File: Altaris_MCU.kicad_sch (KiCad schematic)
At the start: 80 parts, among them J1 Screw_Terminal_01x02, J10 USB_C_Receptacle_USB2.0_16P, J11 Screw_Terminal_01x02, J2 Conn_01x04_Pin, J3 Screw_Terminal_01x02, J4 Screw_Terminal_01x02, J5 Conn_01x04_Pin, J6 Conn_01x04_Pin, J7 Conn_01x08_Socket, J8 Screw_Terminal_01x02, J9 USB_C_Receptacle_USB2.0_16P, Q1 Q_NMOS, SW2 RESET1, SW3 BOOT1, U1 ESP32-S3-WROOM-1, U10 USBLC6-2SC6, U11 MAX31855KASA, U12 TPS62827DMQT, U15 CH340X, U2 MAX31855KASA, U3 TPS79333-EP, U4 ICM-20948, U5 TPS79318-EP, U6 SN74AVC4T774RSVR, U7 MAX31855KASA, U8 MAX31855KASA, U9 SN74AVC4T774RSVR

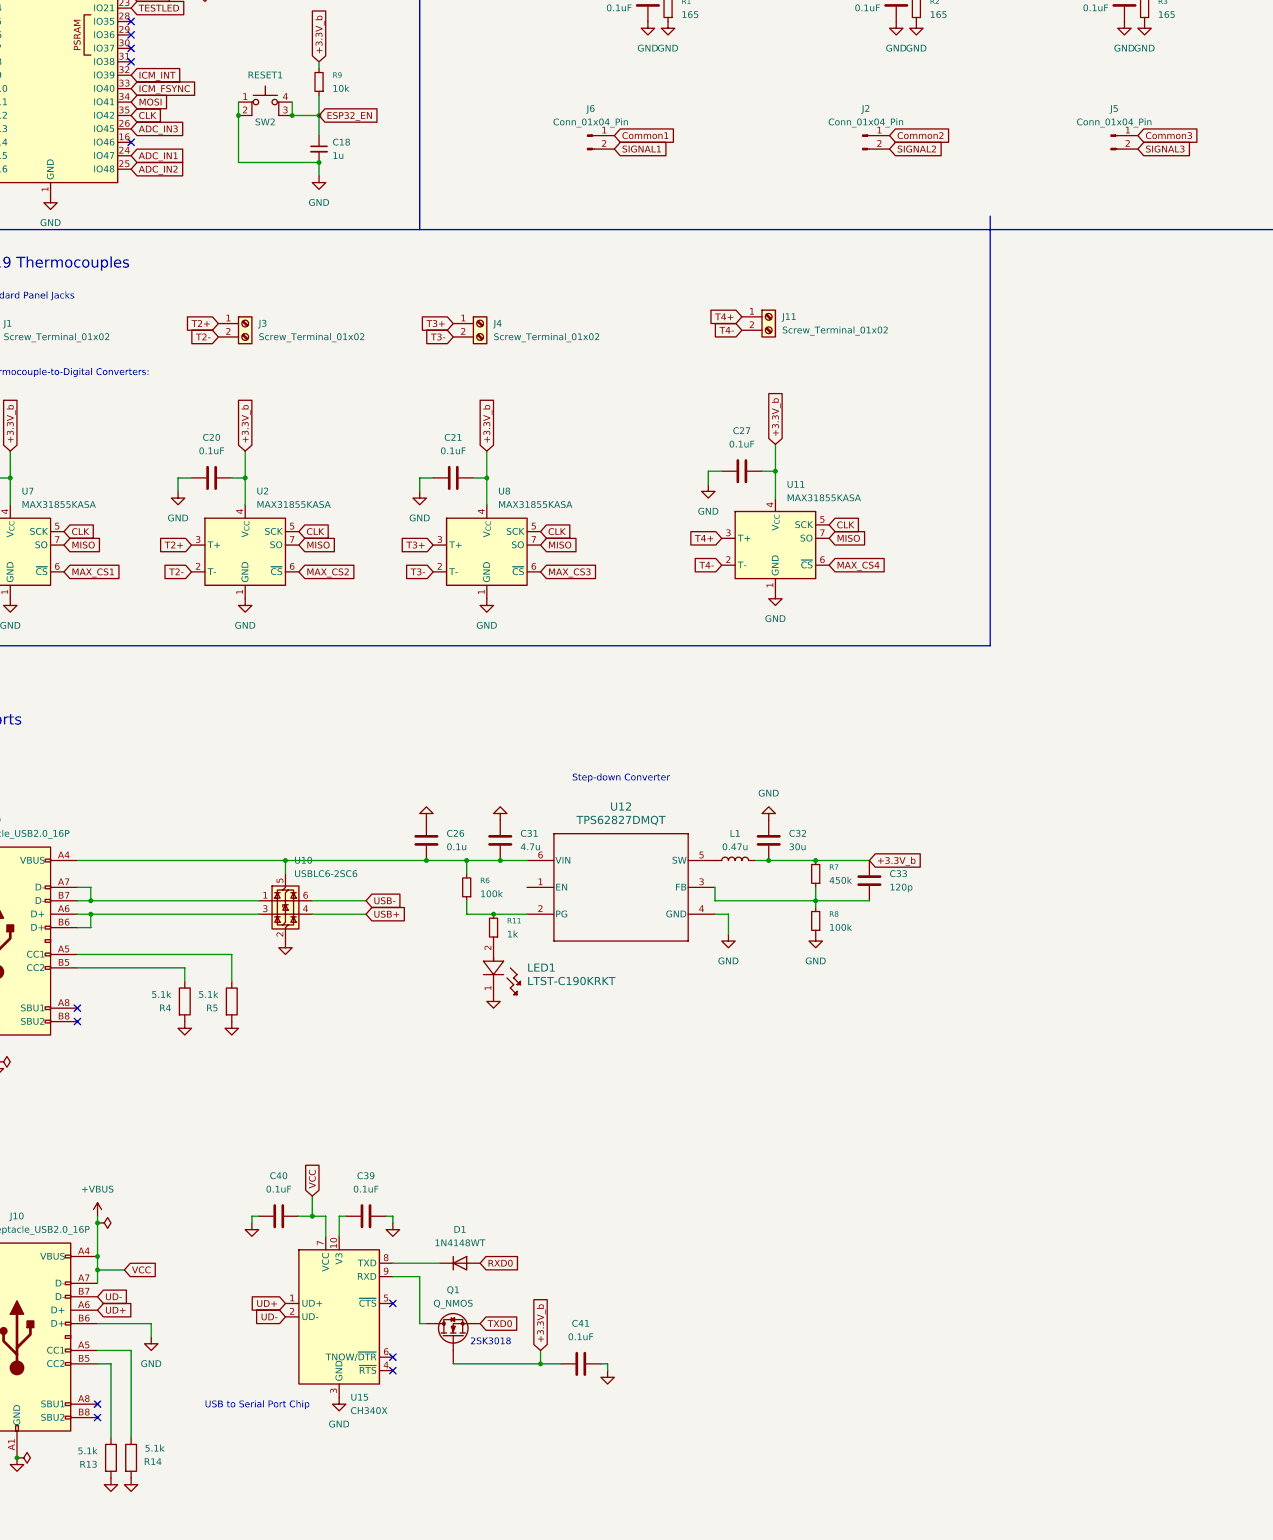
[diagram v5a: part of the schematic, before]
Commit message: Fixed second USB port wiring, changed to screw terminals
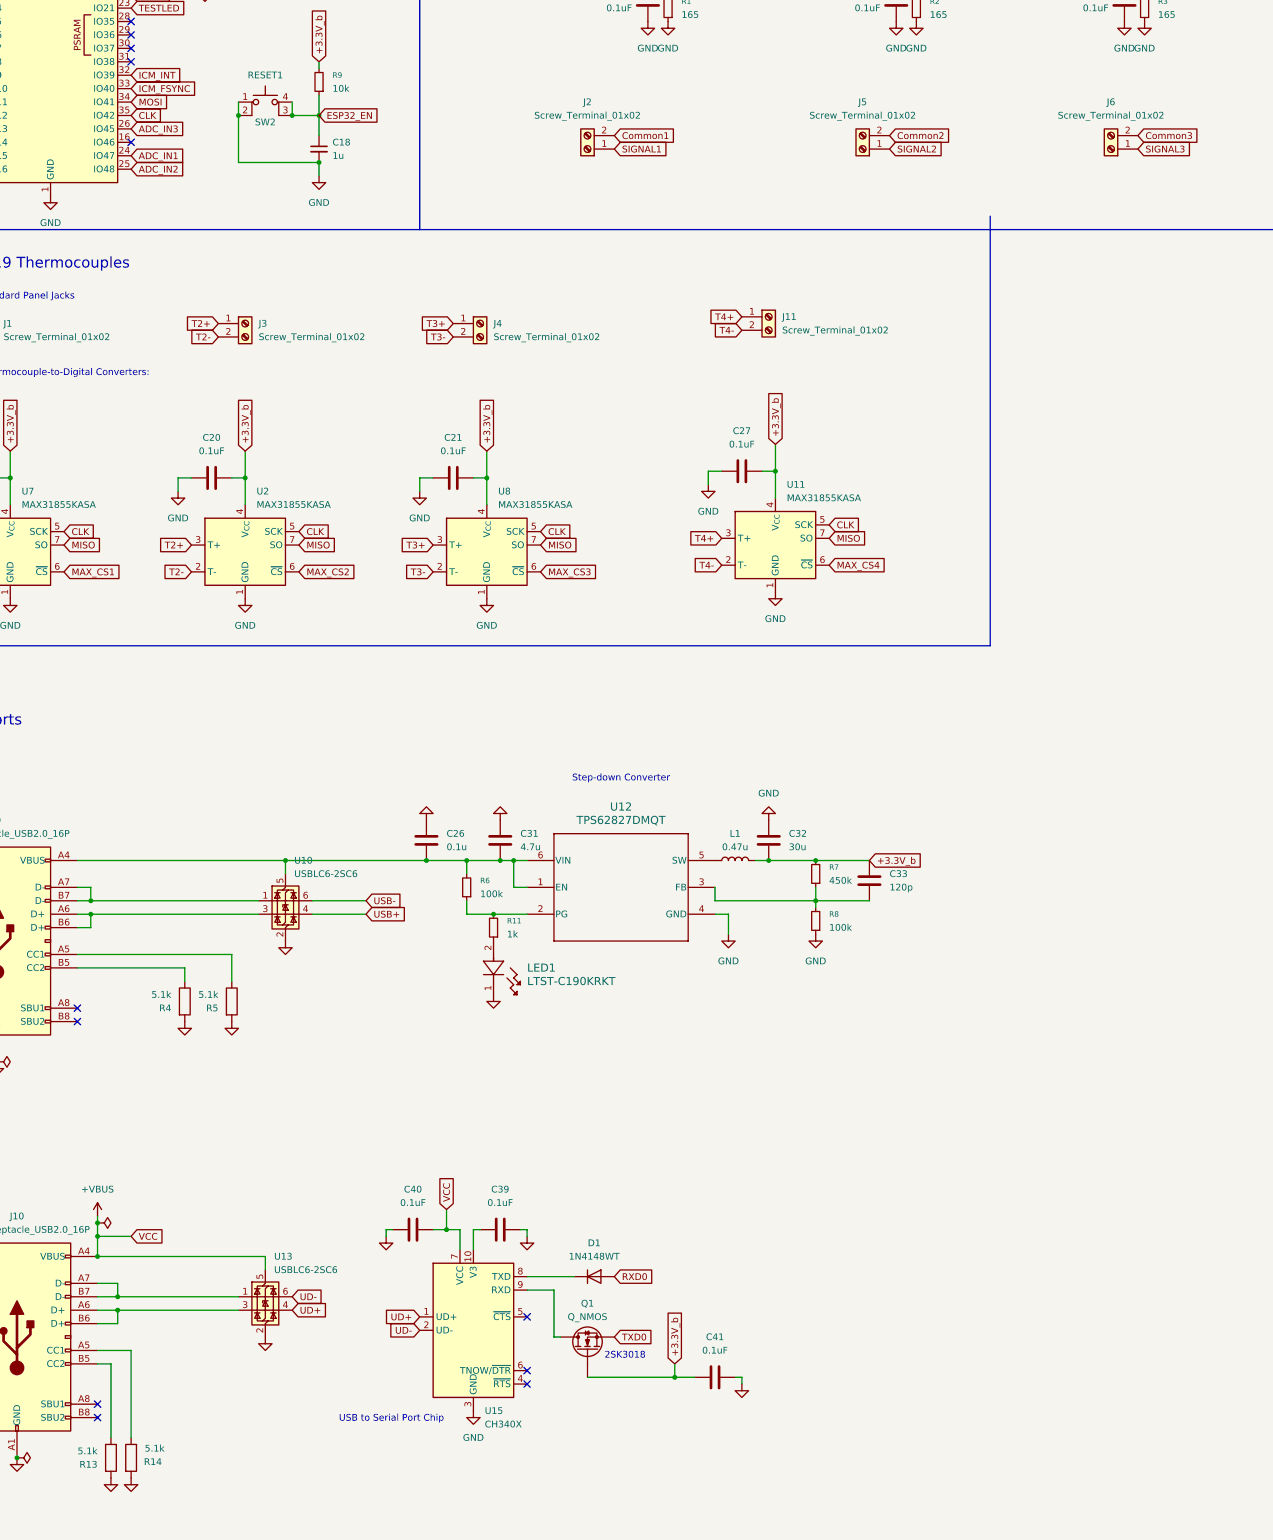
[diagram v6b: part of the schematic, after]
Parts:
- removed J2, J5, J6: Conn_01x04_Pin, TerminalBlock:TerminalBlock_MaiXu_MX126-5.0-02P_1x02_P5.00mm, symbol Connector:Conn_01x02_Pin
- added J2, J5, J6: Screw_Terminal_01x02, TerminalBlock:TerminalBlock_MaiXu_MX126-5.0-02P_1x02_P5.00mm, symbol Connector:Screw_Terminal_01x02
- added U13: USBLC6-2SC6, Package_TO_SOT_SMD:SOT-23-6, symbol Power_Protection:USBLC6-2SC6
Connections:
- net +VBUS: now also U13.5 (VBUS); no longer J10.A7 (D-)
- net ADC_IN1: now also J2.1 (Pin_1)
- net ADC_IN2: now also J5.1 (Pin_1)
- net ADC_IN3: now also J6.1 (Pin_1)
- net Common1: now also J2.2 (Pin_2)
- net Common2: now also J5.2 (Pin_2)
- net Common3: now also J6.2 (Pin_2)
- net GND: now also U13.2 (GND); no longer J10.B6 (D+)
- net UD+: now also U13.4 (I/O2); no longer J10.A6 (D+)
- net UD-: now also U13.6 (I/O1); no longer J10.B7 (D-)
- net at C26.2, C31.2, J9.A4 (VBUS)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: now also U12.1 (EN)
- new net: J10.A7 (D-), J10.B7 (D-), U13.1 (I/O1)
- new net: J10.A6 (D+), J10.B6 (D+), U13.3 (I/O2)
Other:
- moved on the sheet: C39, C40, C41, D1, Q1, U15
